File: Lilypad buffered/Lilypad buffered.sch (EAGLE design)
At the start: 45 parts, among them T1 MMBTA3904, T10 MMBTA3904, T11 MMBTA3906, T12 MMBTA3904, T13 MMBTA3906, T14 MMBTA3904, T15 MMBTA3906, T16 MMBTA3904, T2 MMBTA3906, T3 MMBTA3906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

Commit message: Cambiado el formato de las perforaciones de Excellon a gerber-RS274X. - Actualizados los gerber involucrados. - Actualizado archivo cam involucrado. - Mejoras menores a la tarjeta de Lilypad con bufferes.
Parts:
- removed JP1: (no value), pinhead:PINHD-2X3
- removed R13, R14, R15, R16: 470, resistor:R-EU_R0603
- removed T13, T15: MMBTA3906, transistor:MMBT3906LT1-PNP-SOT23-BEC
- removed T14, T16: MMBTA3904, transistor-neu-to92:MMBT3904LT1-NPN-SOT23-BEC
- removed U$7: 7, LilyPad-Wearables:SEWTAP9
- removed U$8: 8, LilyPad-Wearables:SEWTAP9
- added C1: (no value), rcl:C-EUC0603
- added J1: AVR_SPI_PRG_6PTH, SparkFun-Connectors:AVR_SPI_PRG_6PTH
- added J2: (no value), SparkFun-Connectors:JST_2MM_MALE
- added U2: MIC5219-3.3BM5, SparkFun-PowerIC:MIC52053.3V
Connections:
- removed net N$31: T13.C, T14.C, U$7.1
- removed net N$32: R13.1
- removed net N$33: R14.1
- removed net N$34: R16.2, T16.B
- removed net N$35: R15.2, T15.B
- removed net N$36: T15.C, T16.C, U$8.1
- removed net N$37: R15.1
- removed net N$38: R16.1
- net +3V3: no longer T13.E, T15.E
- net GND: now also C1.2, J2.-, U2.GND; no longer T14.E, T16.E
- net N$29: now also C1.1, U2.BP; no longer R14.2, T14.B
- net N$30: now also J2.+, U2.IN; no longer R13.2, T13.B

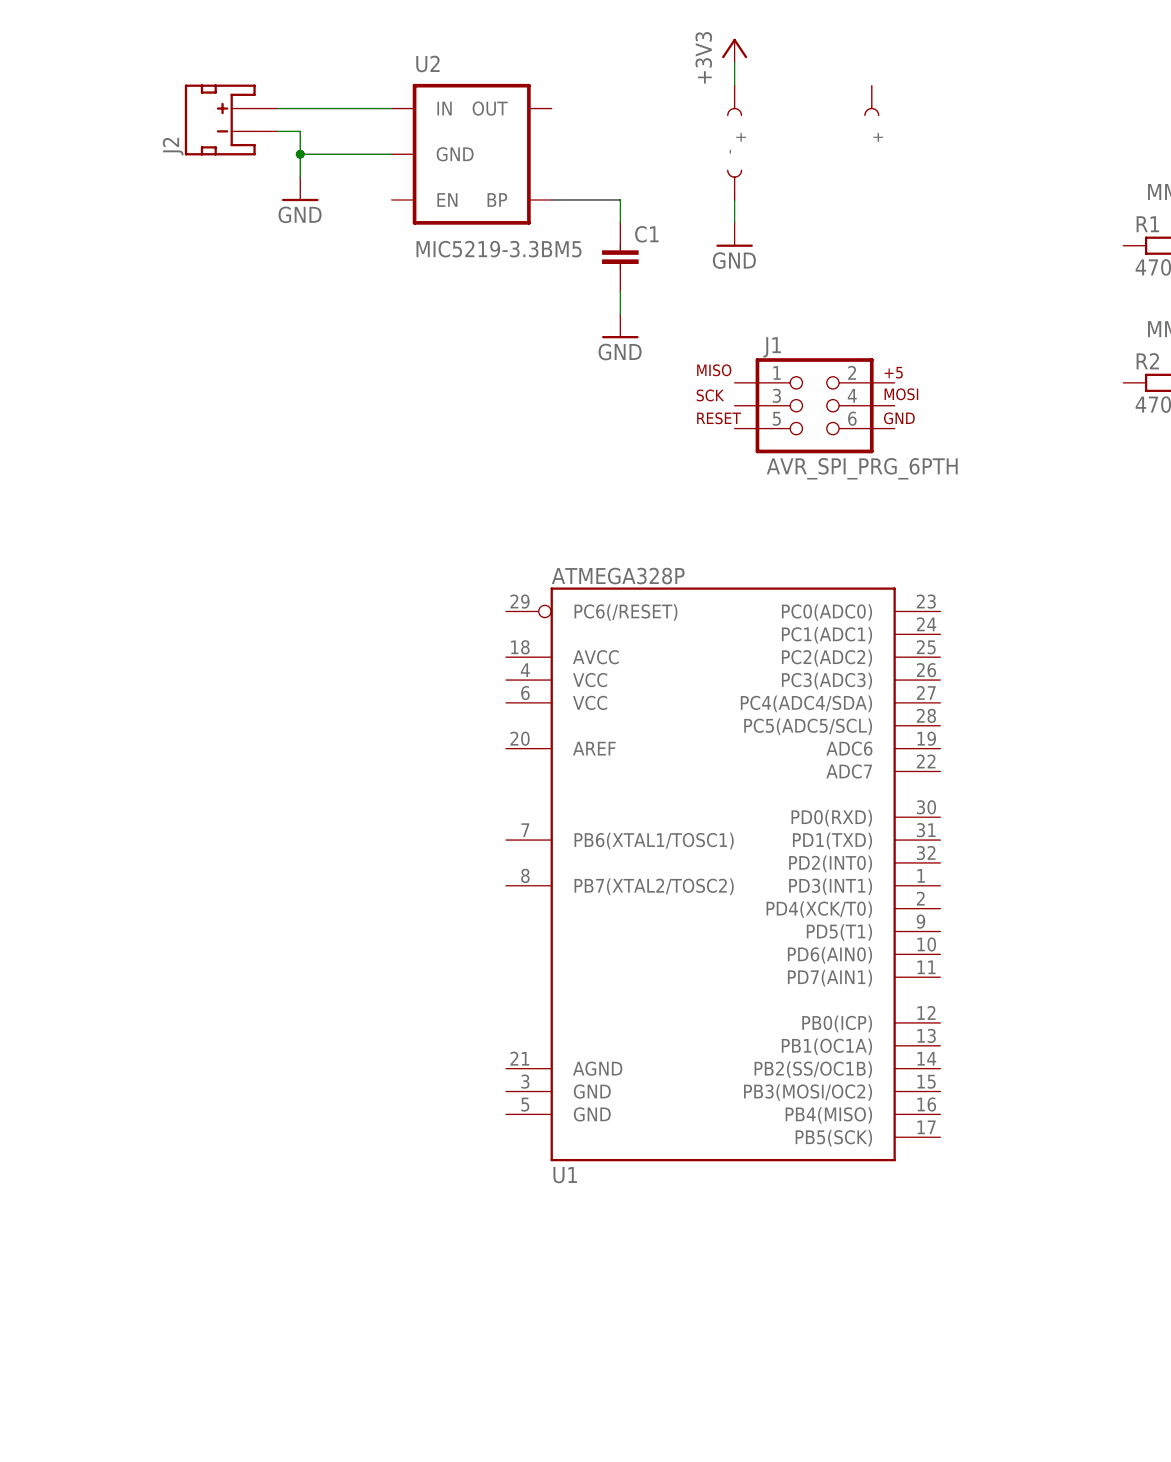
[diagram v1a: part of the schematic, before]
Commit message: Continuado el trabajo sobre el esquematico. Terminado sistema minimo y fuente de suministro (con proteccion).
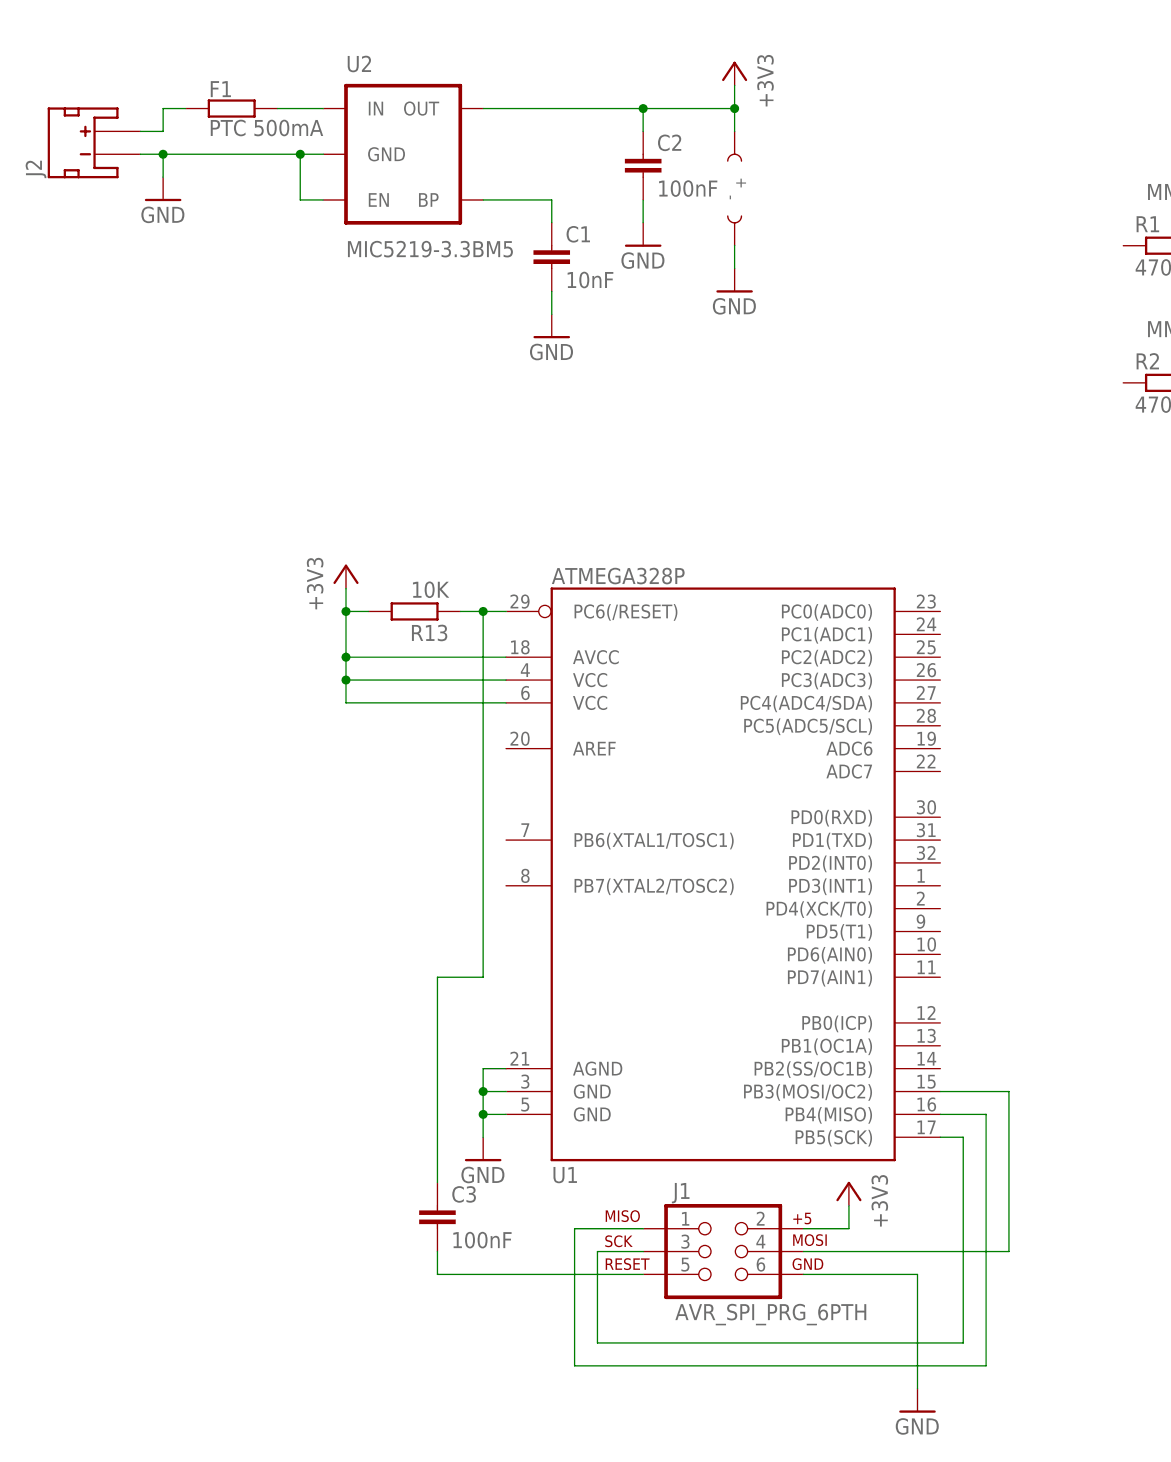
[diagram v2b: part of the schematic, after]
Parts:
- removed U$11: +, LilyPad-Wearables:SEWTAP9
- added C2, C3: 100nF, rcl:C-EUC0805K
- added F1: PTC 500mA, Personal - Varios:RESISTENCIA-SMD-2012
- added R13: 10K, resistor:R-EU_R0603
- C1: value (none) -> 10nF; device rcl:C-EUC0603 -> rcl:C-EUC0805K
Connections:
- new net N$31: J1.3, U1.PB5(SCK)
- new net N$32: J1.1, U1.PB4(MISO)
- new net N$33: J1.4, U1.PB3(MOSI/OC2)
- new net N$34: C3.1, R13.1, U1.PC6(/RESET)
- new net N$35: F1.P$1, U2.IN
- new net N$36: C3.2, J1.5
- net +3V3: now also C2.1, J1.2, R13.2, U1.AVCC, U1.VCC@1, U1.VCC@2, U2.OUT
- net GND: now also C2.2, J1.6, U1.AGND, U1.GND@1, U1.GND@2, U2.EN
- net N$30: now also F1.P$2; no longer U2.IN
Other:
- moved on the sheet: C1, J1, J2, U2
